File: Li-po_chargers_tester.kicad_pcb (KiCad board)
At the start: 2 copper layers, 50 x 50 mm, 42 parts, among them J1 Conn_01x04_Pin, J2 USB_C_Receptacle_PowerOnly_6P, SW1 SW_DIP_x04, U1 BQ24073RGT, U2 MCP73831-3-OT, U3 MCP73833-xxx-MF

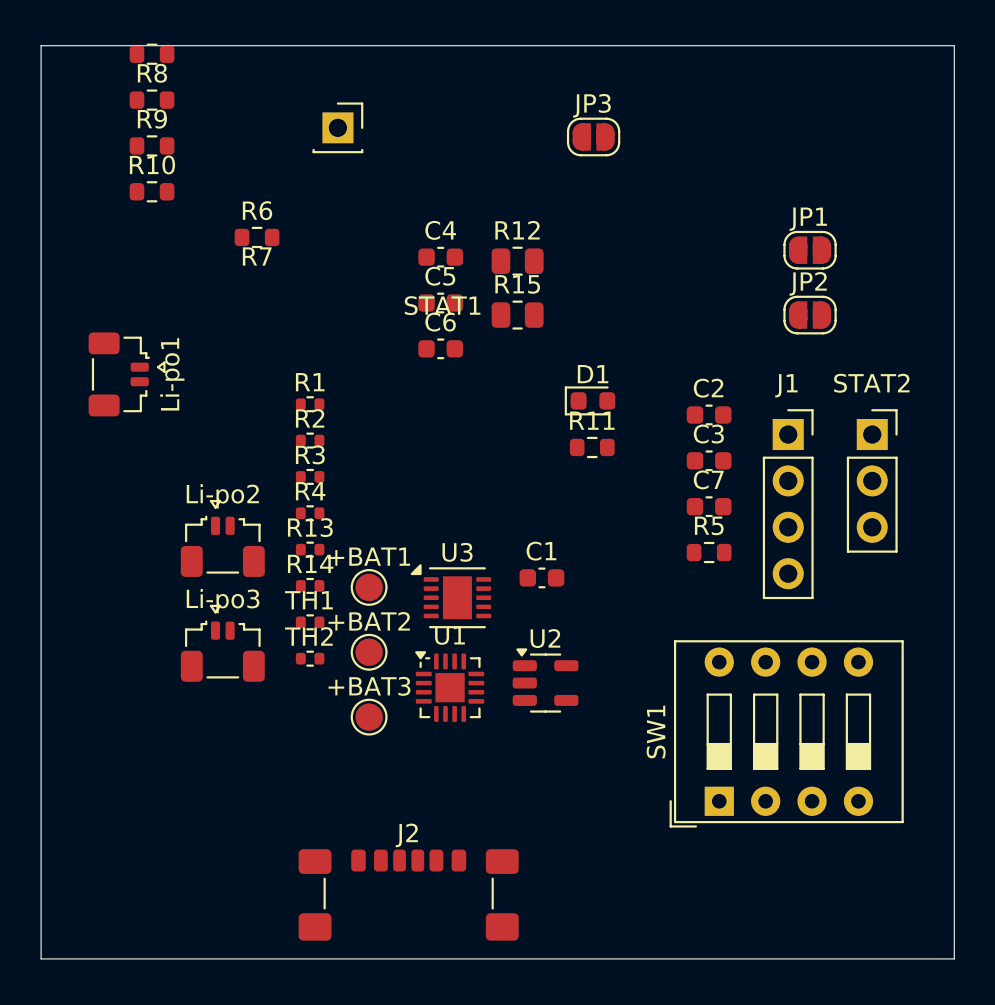
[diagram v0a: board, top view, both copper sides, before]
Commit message: Board making #1 I made the whole PCB board. Just minor bug repairment and then it should be good
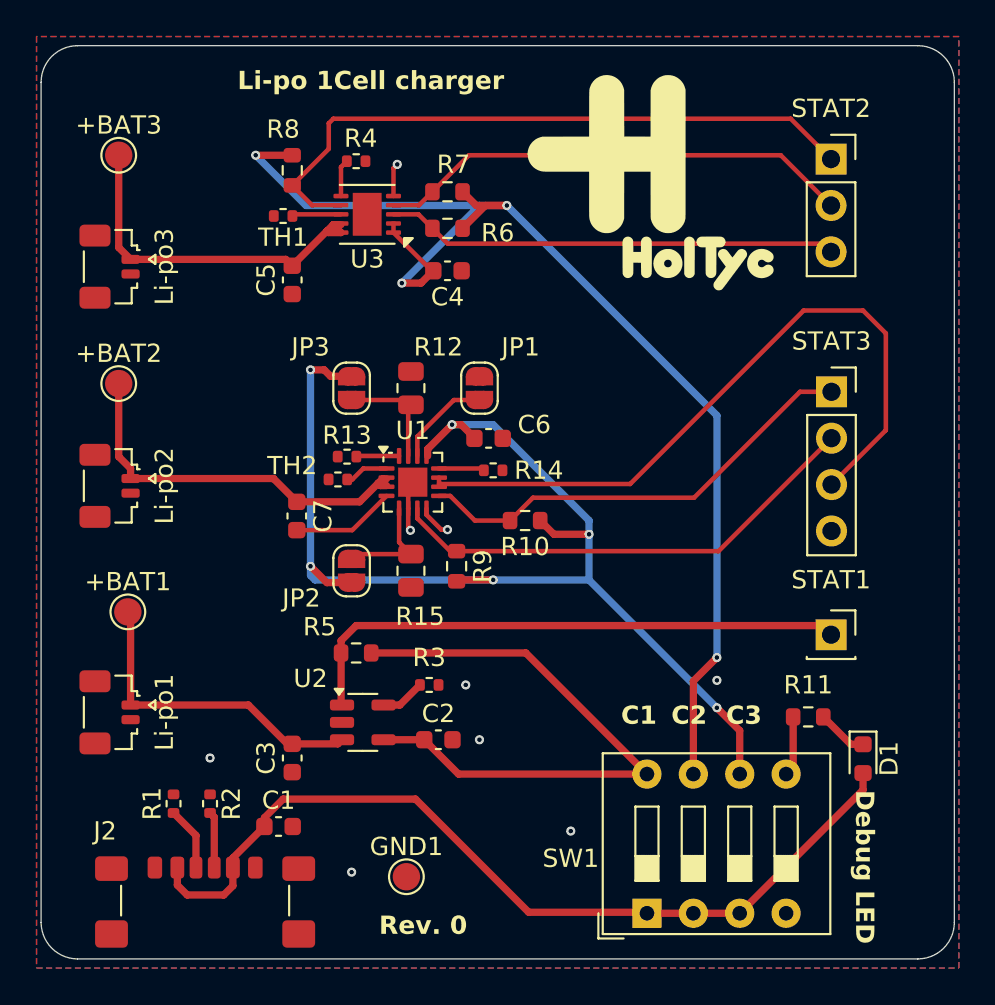
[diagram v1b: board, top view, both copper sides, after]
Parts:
- removed J1: Conn_01x04_Pin, Connector_PinSocket_2.54mm:PinSocket_1x04_P2.54mm_Vertical
- added G***: LOGO, LOGO, F.Cu at (173.5, 64.2)
- added GND1: GND, TestPoint:TestPoint_Pad_D1.5mm, F.Cu at (159.2, 102.0)
- added STAT3: Conn_01x04_Pin, Connector_PinSocket_2.54mm:PinSocket_1x04_P2.54mm_Vertical, F.Cu at (182.5, 75.5)
- moved STAT1 38.7 mm to (182.5, 88.8)
- moved +BAT3 33.7 mm to (143.5, 62.5)
- moved JP2 28.7 mm to (156.2, 85.2), turned to 90 degrees
- moved R9 28.4 mm to (162.0, 85.0), turned to -90 degrees
- moved C3 28.0 mm to (153.0, 95.5), turned to 90 degrees
- moved R10 27.2 mm to (165.8, 82.5), turned to 180 degrees
- moved D1 24.5 mm to (184.2, 95.5), turned to -90 degrees
- moved C2 23.1 mm to (161.0, 94.5)
- moved R1 23.1 mm to (146.5, 98.0), turned to 90 degrees
- moved C7 22.6 mm to (153.2, 82.2), turned to -90 degrees
- moved TH1 22.3 mm to (152.5, 65.8), turned to 180 degrees
- moved Li-po3 22.0 mm to (143.0, 68.6), turned to -90 degrees
- moved U3 21.6 mm to (157.1, 65.7), turned to 180 degrees
- moved R2 20.6 mm to (148.5, 98.0), turned to -90 degrees
- moved +BAT2 20.1 mm to (143.5, 75.0)
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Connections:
- R6 pad 2: Net-(STAT2-Pin_1) -> Net-(STAT2-Pin_3)
- R8 pad 2: Net-(STAT2-Pin_3) -> Net-(STAT2-Pin_1)
- U3 pad 3: Net-(STAT2-Pin_1) -> Net-(STAT2-Pin_3)
- U3 pad 7: Net-(STAT2-Pin_3) -> Net-(STAT2-Pin_1)
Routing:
- net Vbus_2: track 0.00 -> 70.6 mm, vias 0 -> 4
- net Vbus_3: track 0.00 -> 67.4 mm, vias 0 -> 6
- net VBUS: track 0.00 -> 48.4 mm
- net OUT: track 0.00 -> 38.9 mm
- net Net-(STAT2-Pin_1): track 0.00 -> 35.9 mm
- net Vbus_1: track 0.00 -> 33.0 mm
- net Net-(STAT1-Pin_1): track 0.00 -> 30.9 mm
- net Net-(STAT3-Pin_2): track 0.00 -> 26.5 mm
- net Net-(STAT2-Pin_2): track 0.00 -> 26.2 mm
- net Net-(STAT3-Pin_1): track 0.00 -> 25.0 mm
- net Net-(STAT2-Pin_3): track 0.00 -> 24.8 mm
- net +BATT1: track 0.00 -> 21.0 mm
- net +BATT2: track 0.00 -> 20.0 mm
- net +BATT: track 0.00 -> 17.7 mm
- net GND: track 0.00 -> 12.1 mm, vias 0 -> 9
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- added copper zone on B.Cu, net GND
- added copper zone on F.Cu, net GND
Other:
- outline, holes or cut-outs redrawn
- board text added: "C1"
- board text added: "C2"
- board text added: "C3"
- board text added: "Debug LED"
- board text added: "Ho Ho"
- board text added: "JLCJLCJLCJLC"
- board text added: "Li-po 1Cell charger"
- board text added: "Rev. 0"
